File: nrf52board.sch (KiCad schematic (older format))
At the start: 47 parts, among them J1 Conn_01x04, J2 USB_B_Micro, J3 Battery, Q1 Q_PMOS_DSG, SW1 SW_Push, U1 nrf52board, U2 E73-2G4M04S, U3 MCP73831-2-OT, U4 LP2985-3.3, U5 RFM95W-868S2, U6 CP2102-GM

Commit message: pcb: half way through
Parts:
- gave numbers to parts that had none: 3
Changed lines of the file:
@@
 	850  2700 1450 2700
 $Comp
-L Switch:SW_Push SW?
+L Switch:SW_Push SW2
 U 1 1 5B4C7829
 P 10300 4300
-F 0 "SW?" H 10300 4585 50  0000 C CNN
+F 0 "SW2" H 10300 4585 50  0000 C CNN
 F 1 "SW_Push" H 10300 4494 50  0000 C CNN
 F 2 "Button_Switch_SMD:Panasonic_EVQPUJ_EVQPUA" H 10300 4500 50  0001 C CNN
@@
 	10000 4300 10100 4300
 $Comp
-L power:GND #PWR?
+L power:GND #PWR0119
 U 1 1 5B4C7832
 P 10600 4300
-F 0 "#PWR?" H 10600 4050 50  0001 C CNN
+F 0 "#PWR0119" H 10600 4050 50  0001 C CNN
 F 1 "GND" H 10605 4127 50  0000 C CNN
 F 2 "" H 10600 4300 50  0001 C CNN
@@
 P0.18
 $Comp
-L power:+3V3 #PWR?
+L power:+3V3 #PWR0120
 U 1 1 5B5037E9
 P 10800 5650
-F 0 "#PWR?" H 10800 5500 50  0001 C CNN
+F 0 "#PWR0120" H 10800 5500 50  0001 C CNN
 F 1 "+3V3" H 10815 5823 50  0000 C CNN
 F 2 "" H 10800 5650 50  0001 C CNN
@@
 $EndComp
 $Comp
-L Device:LED D?
+L Device:LED D4
 U 1 1 5B5037EF
 P 10150 5650
-F 0 "D?" H 10141 5866 50  0000 C CNN
+F 0 "D4" H 10141 5866 50  0000 C CNN
 F 1 "LED" H 10141 5775 50  0000 C CNN
 F 2 "LED_SMD:LED_0603_1608Metric" H 10150 5650 50  0001 C CNN
@@
 $EndComp
 $Comp
-L Device:R R?
+L Device:R R9
 U 1 1 5B5037F5
 P 10550 5650
-F 0 "R?" H 10620 5696 50  0000 L CNN
+F 0 "R9" H 10620 5696 50  0000 L CNN
 F 1 "1k" H 10620 5605 50  0000 L CNN
 F 2 "Resistor_SMD:R_0603_1608Metric" V 10480 5650 50  0001 C CNN

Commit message: sch: rescue
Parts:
- J2: symbol Connector_Specialized:USB_B_Micro -> nrf52board-rescue:USB_B_Micro-Connector_Specialized
- U5: symbol RF_AM_FM:RFM95W-868S2 -> nrf52board-rescue:RFM95W-868S2-RF_AM_FM
- U6: symbol usb-uart:CP2102-GM -> nrf52board-rescue:CP2102-GM-usb-uart
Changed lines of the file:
@@
 EESchema Schematic File Version 4
 LIBS:nrf52board-cache
-EELAYER 26 0
+EELAYER 30 0
 EELAYER END
 $Descr A4 11693 8268
@@
 	7800 1200 7950 1200
 $Comp
-L RF_AM_FM:RFM95W-868S2 U5
+L nrf52board-rescue:RFM95W-868S2-RF_AM_FM U5
 U 1 1 5AC451EB
 P 5550 1650
@@
 $EndComp
 $Comp
-L Connector_Specialized:USB_B_Micro J2
+L nrf52board-rescue:USB_B_Micro-Connector_Specialized J2
 U 1 1 5AD0C80B
 P 1150 3550
@@
 	4650 4050 5550 4050
 $Comp
-L usb-uart:CP2102-GM U6
+L nrf52board-rescue:CP2102-GM-usb-uart U6
 U 1 1 5B070B6B
 P 5900 5450

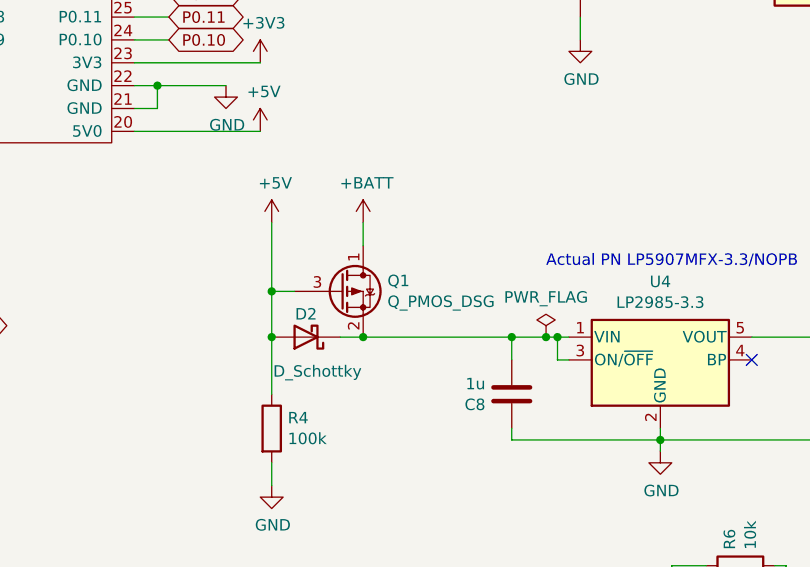
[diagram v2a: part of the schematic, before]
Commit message: Change Q1 to PMV65XP
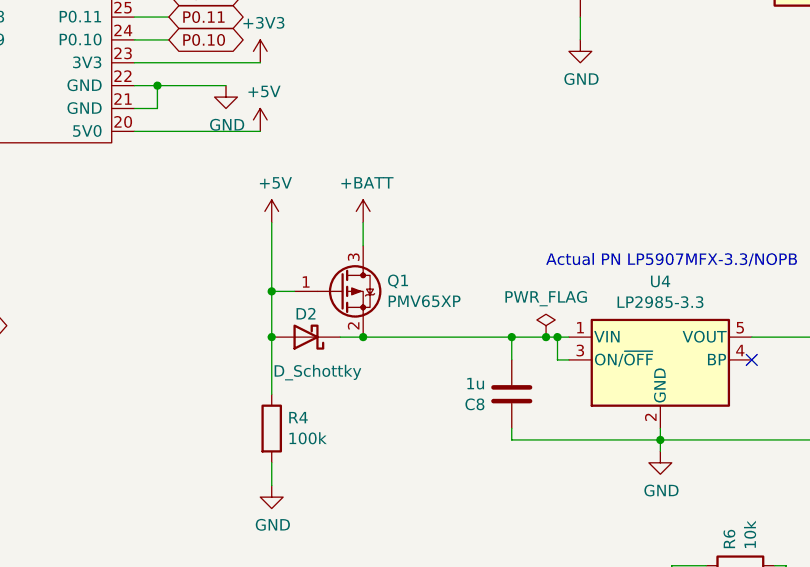
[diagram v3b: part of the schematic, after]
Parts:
- removed Q1: Q_PMOS_DSG, Package_TO_SOT_SMD:SOT-23, symbol Device:Q_PMOS_DSG
- added Q1: PMV65XP, symbol Device:Q_PMOS_GSD
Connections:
- net +5V: now also Q1.1 (G)
- net +BATT: now also Q1.3 (D)
- net at C8.2, D2.1 (K), U4.1 (VIN)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: now also Q1.2 (S)
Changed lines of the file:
@@
 EESchema Schematic File Version 4
-LIBS:nrf52board-cache
 EELAYER 30 0
 EELAYER END
@@
 	1    0    0    -1
 $EndComp
-$Comp
-L Device:Q_PMOS_DSG Q1
-U 1 1 5AF40185
-P 3250 3400
-F 0 "Q1" H 3456 3446 50  0000 L CNN
-F 1 "Q_PMOS_DSG" H 3456 3355 50  0000 L CNN
-F 2 "Package_TO_SOT_SMD:SOT-23" H 3450 3500 50  0001 C CNN
-F 3 "~" H 3250 3400 50  0001 C CNN
-	1    3250 3400
-	1    0    0    -1
-$EndComp
 Wire Wire Line
 	3350 3100 3350 3200
@@
 Wire Wire Line
 	2950 4150 2950 4250
-Wire Wire Line
-	3350 3600 4000 3600
 Connection ~ 4000 3600
 $Comp
@@
 	2950 3600 2950 3850
 Connection ~ 2950 3600
-Wire Wire Line
-	3250 3600 3350 3600
-Connection ~ 3350 3600
 Text GLabel 4950 1350 0    50   Input ~ 0
 P0.25
@@
 Wire Wire Line
 	10700 5650 10800 5650
+Wire Wire Line
+	3250 3600 3350 3600
+$Comp
+L Device:Q_PMOS_GSD Q1
+U 1 1 6046DA55
+P 3250 3400
+F 0 "Q1" H 3455 3446 50  0000 L CNN
+F 1 "PMV65XP" H 3455 3355 50  0000 L CNN
+F 2 "" H 3450 3500 50  0001 C CNN
+F 3 "~" H 3250 3400 50  0001 C CNN
+	1    3250 3400
+	1    0    0    -1
+$EndComp
+Connection ~ 3350 3600
+Wire Wire Line
+	3350 3600 4000 3600
 $EndSCHEMATC

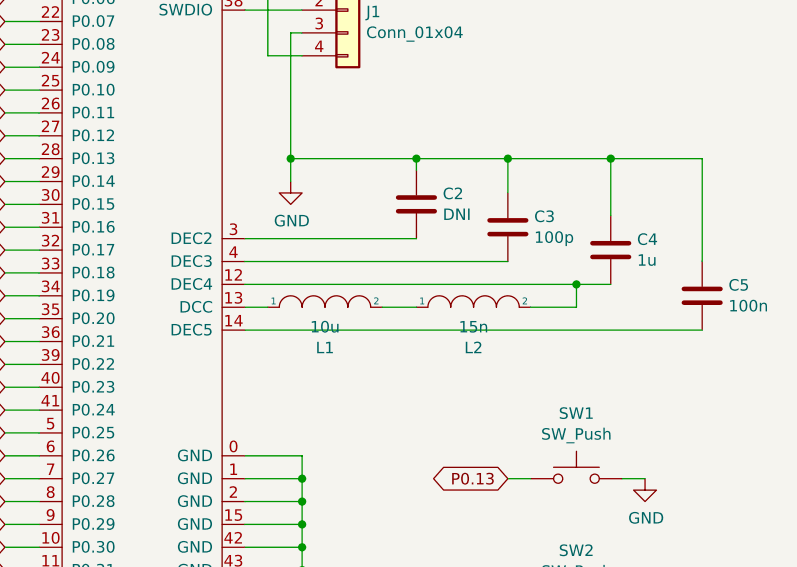
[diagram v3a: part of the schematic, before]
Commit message: Update Q1 on PCB
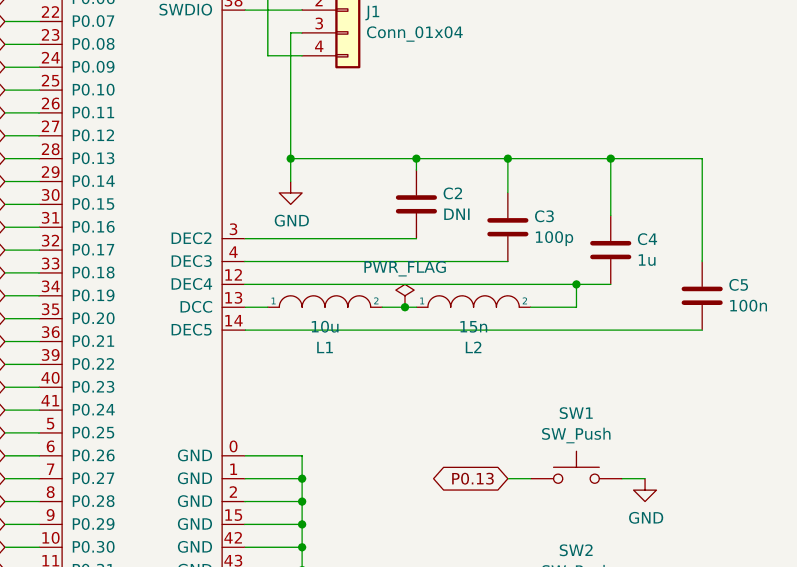
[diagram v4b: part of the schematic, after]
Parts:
- Q1: footprint (none) -> Package_TO_SOT_SMD:SOT-23
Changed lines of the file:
@@
 	8850 2950 8950 2950
 Wire Wire Line
-	9450 2950 9600 2950
+	9450 2950 9550 2950
 Wire Wire Line
 	10100 2950 10300 2950
@@
 Wire Wire Line
 	1050 6250 1450 6250
-Text Notes 1500 6050 0    50   ~ 0
-10k = 100 mA charge
 NoConn ~ 6050 1350
 Wire Wire Line
@@
 Wire Wire Line
 	3250 3600 3350 3600
+Connection ~ 3350 3600
+Wire Wire Line
+	3350 3600 4000 3600
+Text Notes 1500 6050 0    50   ~ 0
+10k = 100 mA charge
 $Comp
 L Device:Q_PMOS_GSD Q1
@@
 F 0 "Q1" H 3455 3446 50  0000 L CNN
 F 1 "PMV65XP" H 3455 3355 50  0000 L CNN
-F 2 "" H 3450 3500 50  0001 C CNN
+F 2 "Package_TO_SOT_SMD:SOT-23" H 3450 3500 50  0001 C CNN
 F 3 "~" H 3250 3400 50  0001 C CNN
 	1    3250 3400
 	1    0    0    -1
 $EndComp
-Connection ~ 3350 3600
-Wire Wire Line
-	3350 3600 4000 3600
+$Comp
+L power:PWR_FLAG #FLG0102
+U 1 1 60474DC0
+P 9550 2950
+F 0 "#FLG0102" H 9550 3025 50  0001 C CNN
+F 1 "PWR_FLAG" H 9550 3124 50  0000 C CNN
+F 2 "" H 9550 2950 50  0001 C CNN
+F 3 "" H 9550 2950 50  0001 C CNN
+	1    9550 2950
+	1    0    0    -1
+$EndComp
+Connection ~ 9550 2950
+Wire Wire Line
+	9550 2950 9600 2950
 $EndSCHEMATC

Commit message: Fix BOM
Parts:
- D1, D3, D4: value LED -> LC191yct
- D2: value D_Schottky -> NSR1020MW2
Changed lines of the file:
@@
 P 2100 5150
 F 0 "D1" H 2092 4895 50  0000 C CNN
-F 1 "LED" H 2092 4986 50  0000 C CNN
+F 1 "LC191yct" H 2092 4986 50  0000 C CNN
 F 2 "LED_SMD:LED_0603_1608Metric" H 2100 5150 50  0001 C CNN
 F 3 "~" H 2100 5150 50  0001 C CNN
@@
 P 3100 3600
 F 0 "D2" H 3100 3500 50  0000 C CNN
-F 1 "D_Schottky" H 3050 3750 50  0000 C CNN
+F 1 "NSR1020MW2" H 3050 3750 50  0000 C CNN
 F 2 "Diode_SMD:D_SOD-323" H 3100 3600 50  0001 C CNN
 F 3 "~" H 3100 3600 50  0001 C CNN
@@
 P 10150 5100
 F 0 "D3" H 10141 5316 50  0000 C CNN
-F 1 "LED" H 10141 5225 50  0000 C CNN
+F 1 "LC191yct" H 10141 5225 50  0000 C CNN
 F 2 "LED_SMD:LED_0603_1608Metric" H 10150 5100 50  0001 C CNN
 F 3 "~" H 10150 5100 50  0001 C CNN
@@
 P 10150 5650
 F 0 "D4" H 10141 5866 50  0000 C CNN
-F 1 "LED" H 10141 5775 50  0000 C CNN
+F 1 "LC191yct" H 10141 5775 50  0000 C CNN
 F 2 "LED_SMD:LED_0603_1608Metric" H 10150 5650 50  0001 C CNN
 F 3 "~" H 10150 5650 50  0001 C CNN

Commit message: add button name
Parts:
- SW1, SW2: value SW_Push -> SKSCLCE010
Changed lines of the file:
@@
 P 10300 3700
 F 0 "SW1" H 10300 3985 50  0000 C CNN
-F 1 "SW_Push" H 10300 3894 50  0000 C CNN
+F 1 "SKSCLCE010" H 10300 3894 50  0000 C CNN
 F 2 "Button_Switch_SMD:Panasonic_EVQPUJ_EVQPUA" H 10300 3900 50  0001 C CNN
 F 3 "" H 10300 3900 50  0001 C CNN
@@
 P 10300 4300
 F 0 "SW2" H 10300 4585 50  0000 C CNN
-F 1 "SW_Push" H 10300 4494 50  0000 C CNN
+F 1 "SKSCLCE010" H 10300 4494 50  0000 C CNN
 F 2 "Button_Switch_SMD:Panasonic_EVQPUJ_EVQPUA" H 10300 4500 50  0001 C CNN
 F 3 "" H 10300 4500 50  0001 C CNN
